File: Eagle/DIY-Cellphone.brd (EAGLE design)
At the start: 130.8 x 58.4 mm, 68 parts, among them IC1 MEGA1284, J1 ISP, U1 MCP73831, U7 M10_HDWITHOUT_EXCLUSION, X1 BU-SMA-V, X3 CCM03-3002 R102

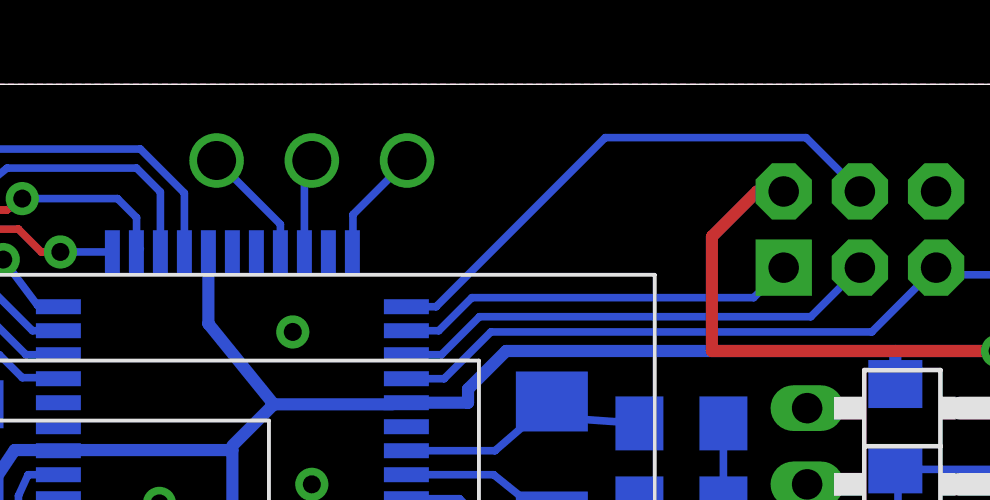
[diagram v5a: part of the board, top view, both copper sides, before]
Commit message: Break out additional microcontroller pins.
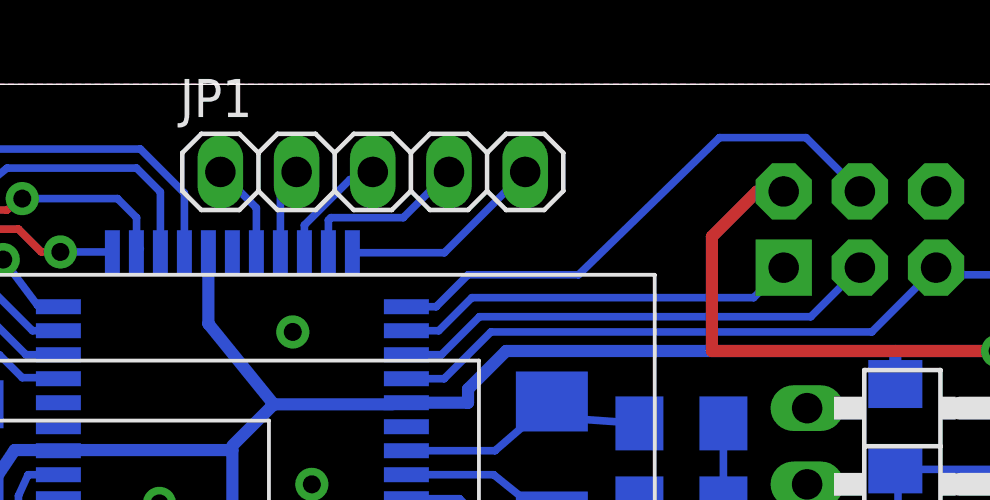
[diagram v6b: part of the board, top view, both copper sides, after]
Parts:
- added JP1: (no value), pinhead:1X05
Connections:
- new net N$38: IC1.40, JP1.1
- new net N$39: IC1.41, JP1.2
- new net N$40: IC1.42, JP1.3
- new net N$41: IC1.43, JP1.4
- new net N$42: IC1.44, JP1.5
- net DTR: no longer IC1.41
- net RI: no longer IC1.42
- net STATUS: no longer IC1.44
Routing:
- net N$42: track 0.00 -> 6.88 mm
- net N$41: track 0.00 -> 5.77 mm
- net DTR: track 3.96 -> 0.00 mm, vias 1 -> 0
- net N$40: track 0.00 -> 3.93 mm
- net STATUS: track 28.0 -> 24.2 mm, vias 1 -> 0
- net N$38: track 0.00 -> 3.19 mm
- net RI: track 3.18 -> 0.00 mm, vias 1 -> 0
- net N$39: track 0.00 -> 2.92 mm
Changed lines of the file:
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@@
 <attribute name="VALUE" x="74.93" y="3.175" size="0.8128" layer="28" rot="MR180"/>
 </element>
+<element name="JP1" library="pinhead" package="1X05" value="" x="106.172" y="55.499"/>
 </elements>
 <signals>
@@
 <signal name="DTR">
 <contactref element="U7" pad="P$59"/>
-<contactref element="IC1" pad="41"/>
-<via x="100.965" y="55.88" extent="1-16" drill="1.3" shape="octagon"/>
-<wire x1="100.965" y1="55.88" x2="103.092" y2="53.753" width="0.254" layer="16"/>
-<wire x1="103.092" y1="53.753" x2="103.092" y2="52.806" width="0.254" layer="16"/>
-<wire x1="59.665" y1="28.024" x2="100.965" y2="55.88" width="0" layer="19" extent="16-16"/>
 </signal>
 <signal name="GPIO0">
@@
 <signal name="STATUS">
 <contactref element="U7" pad="P$54"/>
-<contactref element="IC1" pad="44"/>
-<via x="107.315" y="55.88" extent="1-16" drill="1.3" shape="octagon"/>
-<wire x1="105.492" y1="52.806" x2="105.511" y2="52.806" width="0.254" layer="16"/>
-<wire x1="105.511" y1="52.806" x2="105.511" y2="54.076" width="0.254" layer="16"/>
-<wire x1="105.511" y1="54.076" x2="107.315" y2="55.88" width="0.254" layer="16"/>
 <contactref element="LED2" pad="A"/>
 <wire x1="59.665" y1="21.524" x2="67.376" y2="21.524" width="0.254" layer="16"/>
 <wire x1="67.376" y1="21.524" x2="72.39" y2="16.51" width="0.254" layer="16"/>
 <wire x1="72.39" y1="16.51" x2="72.39" y2="7.137" width="0.254" layer="16"/>
-<wire x1="72.39" y1="16.51" x2="105.492" y2="52.806" width="0" layer="19" extent="16-16"/>
 </signal>
 <signal name="SIM_RSTR">
@@
 <signal name="RI">
 <contactref element="U7" pad="P$55"/>
-<contactref element="IC1" pad="42"/>
-<via x="104.14" y="55.88" extent="1-16" drill="1.3" shape="octagon"/>
-<wire x1="104.14" y1="55.88" x2="103.892" y2="55.632" width="0.254" layer="16"/>
-<wire x1="103.892" y1="55.632" x2="103.892" y2="52.806" width="0.254" layer="16"/>
-<wire x1="59.665" y1="22.824" x2="103.892" y2="52.806" width="0" layer="19" extent="16-16"/>
 </signal>
 <signal name="ANTENA" class="4">
@@
 <contactref element="J1" pad="4"/>
 <wire x1="107.292" y1="51.006" x2="108.283" y2="51.006" width="0.254" layer="16"/>
-<wire x1="108.283" y1="51.006" x2="113.919" y2="56.642" width="0.254" layer="16"/>
-<wire x1="113.919" y1="56.642" x2="120.615" y2="56.642" width="0.254" layer="16"/>
+<wire x1="108.283" y1="51.006" x2="109.347" y2="52.07" width="0.254" layer="16"/>
+<wire x1="109.347" y1="52.07" x2="113.03" y2="52.07" width="0.254" layer="16"/>
+<wire x1="113.03" y1="52.07" x2="117.729" y2="56.642" width="0.254" layer="16"/>
+<wire x1="117.729" y1="56.642" x2="120.615" y2="56.642" width="0.254" layer="16"/>
 <wire x1="120.615" y1="56.642" x2="122.409" y2="54.848" width="0.254" layer="16"/>
 </signal>
@@
 <wire x1="72.39" y1="4.293" x2="76.2" y2="4.293" width="0.254" layer="16"/>
 </signal>
+<signal name="N$38">
+<contactref element="IC1" pad="40"/>
+<contactref element="JP1" pad="1"/>
+<wire x1="102.292" y1="52.806" x2="102.292" y2="54.299" width="0.254" layer="16"/>
+<wire x1="102.292" y1="54.299" x2="101.092" y2="55.499" width="0.254" layer="16"/>
+</signal>
+<signal name="N$39">
+<contactref element="IC1" pad="41"/>
+<contactref element="JP1" pad="2"/>
+<wire x1="103.092" y1="52.806" x2="103.092" y2="54.959" width="0.254" layer="16"/>
+<wire x1="103.092" y1="54.959" x2="103.632" y2="55.499" width="0.254" layer="16"/>
+</signal>
+<signal name="N$40">
+<contactref element="IC1" pad="42"/>
+<contactref element="JP1" pad="3"/>
+<wire x1="103.892" y1="52.806" x2="103.892" y2="53.727" width="0.254" layer="16"/>
+<wire x1="103.892" y1="53.727" x2="105.41" y2="55.245" width="0.254" layer="16"/>
+<wire x1="105.41" y1="55.245" x2="105.918" y2="55.245" width="0.254" layer="16"/>
+<wire x1="105.918" y1="55.245" x2="106.172" y2="55.499" width="0.254" layer="16"/>
+</signal>
+<signal name="N$41">
+<contactref element="IC1" pad="43"/>
+<contactref element="JP1" pad="4"/>
+<wire x1="104.692" y1="52.806" x2="104.692" y2="53.892" width="0.254" layer="16"/>
+<wire x1="104.692" y1="53.892" x2="104.775" y2="53.975" width="0.254" layer="16"/>
+<wire x1="104.775" y1="53.975" x2="107.188" y2="53.975" width="0.254" layer="16"/>
+<wire x1="107.188" y1="53.975" x2="108.712" y2="55.499" width="0.254" layer="16"/>
+</signal>
+<signal name="N$42">
+<contactref element="IC1" pad="44"/>
+<contactref element="JP1" pad="5"/>
+<wire x1="105.492" y1="52.806" x2="108.559" y2="52.806" width="0.254" layer="16"/>
+<wire x1="108.559" y1="52.806" x2="111.252" y2="55.499" width="0.254" layer="16"/>
+</signal>
 </signals>

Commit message: Remove RTS/CTS connection on M10.
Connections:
- new net N$43: U7.P$58
- net N$1: no longer U7.P$58
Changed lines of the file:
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@@
 <signal name="N$1">
 <contactref element="U7" pad="P$57"/>
-<contactref element="U7" pad="P$58"/>
-<wire x1="59.665" y1="26.724" x2="59.665" y2="25.424" width="0" layer="19" extent="16-16"/>
 </signal>
 <signal name="DTR">
@@
 <wire x1="108.559" y1="52.806" x2="111.252" y2="55.499" width="0.254" layer="16"/>
 </signal>
+<signal name="N$43">
+<contactref element="U7" pad="P$58"/>
+</signal>
 </signals>
